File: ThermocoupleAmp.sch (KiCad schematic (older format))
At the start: 7 parts

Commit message: Done with preliminary schematic. Needs review
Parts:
- C602: renamed from C?; footprint (none) -> Capacitor_SMD:C_0603_1608Metric
- R601, R602, R603: renamed from R?; footprint (none) -> Resistor_SMD:R_0603_1608Metric
- gave numbers to parts that had none: 3
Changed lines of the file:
@@
 $Descr A4 11693 8268
 encoding utf-8
-Sheet 7 7
+Sheet 6 7
 Title ""
 Date ""
@@
 $EndDescr
 $Comp
-L ReflowOven:MCP96RL01T U?
+L ReflowOven:MCP96RL01T U601
 U 1 1 5F712CB5
 P 5650 3250
-F 0 "U?" H 5650 3815 50  0000 C CNN
+F 0 "U601" H 5650 3815 50  0000 C CNN
 F 1 "MCP96RL01T" H 5650 3724 50  0000 C CNN
 F 2 "" H 5600 3500 50  0001 C CNN
@@
 	4900 2950 4900 2800
 $Comp
-L power:+3.3VA #PWR?
+L power:+3.3VA #PWR0603
 U 1 1 5F716651
 P 4900 2800
-F 0 "#PWR?" H 4900 2650 50  0001 C CNN
+F 0 "#PWR0603" H 4900 2650 50  0001 C CNN
 F 1 "+3.3VA" H 4915 2973 50  0000 C CNN
 F 2 "" H 4900 2800 50  0001 C CNN
@@
 $EndComp
 $Comp
-L power:GNDA #PWR?
+L power:GNDA #PWR0608
 U 1 1 5F7169A0
 P 4900 4300
-F 0 "#PWR?" H 4900 4050 50  0001 C CNN
+F 0 "#PWR0608" H 4900 4050 50  0001 C CNN
 F 1 "GNDA" H 4905 4127 50  0000 C CNN
 F 2 "" H 4900 4300 50  0001 C CNN
@@
 $EndComp
 $Comp
-L Connector:Conn_01x02_Male J?
+L Connector:Conn_01x02_Male J601
 U 1 1 5F71786F
 P 7300 4050
-F 0 "J?" H 7272 3932 50  0000 R CNN
+F 0 "J601" H 7272 3932 50  0000 R CNN
 F 1 "Conn_01x02_Male" H 7272 4023 50  0000 R CNN
 F 2 "" H 7300 4050 50  0001 C CNN
@@
 NoConn ~ 6250 2950
 $Comp
-L power:+3.3VA #PWR?
+L power:+3.3VA #PWR0606
 U 1 1 5F71AC1D
 P 6500 3200
-F 0 "#PWR?" H 6500 3050 50  0001 C CNN
+F 0 "#PWR0606" H 6500 3050 50  0001 C CNN
 F 1 "+3.3VA" H 6515 3373 50  0000 C CNN
 F 2 "" H 6500 3200 50  0001 C CNN
@@
 	6500 3200 6500 3250
 $Comp
-L Device:R_Small R?
+L Device:R_Small R601
 U 1 1 5F71B54E
 P 6500 3350
-F 0 "R?" H 6559 3396 50  0000 L CNN
+F 0 "R601" H 6559 3396 50  0000 L CNN
 F 1 "1M" H 6559 3305 50  0000 L CNN
-F 2 "" H 6500 3350 50  0001 C CNN
+F 2 "Resistor_SMD:R_0603_1608Metric" H 6500 3350 50  0001 C CNN
 F 3 "~" H 6500 3350 50  0001 C CNN
 	1    6500 3350
@@
 	6800 4050 7100 4050
 $Comp
-L Device:R_Small R?
+L Device:R_Small R603
 U 1 1 5F71BB42
 P 6800 4250
-F 0 "R?" H 6859 4296 50  0000 L CNN
+F 0 "R603" H 6859 4296 50  0000 L CNN
 F 1 "2M" H 6859 4205 50  0000 L CNN
-F 2 "" H 6800 4250 50  0001 C CNN
+F 2 "Resistor_SMD:R_0603_1608Metric" H 6800 4250 50  0001 C CNN
 F 3 "~" H 6800 4250 50  0001 C CNN
 	1    6800 4250
@@
 $EndComp
 $Comp
-L Device:R_Small R?
+L Device:R_Small R602
 U 1 1 5F71BF24
 P 6800 3600
-F 0 "R?" V 6604 3600 50  0000 C CNN
+F 0 "R602" V 6604 3600 50  0000 C CNN
 F 1 "2M" V 6695 3600 50  0000 C CNN
-F 2 "" H 6800 3600 50  0001 C CNN
+F 2 "Resistor_SMD:R_0603_1608Metric" H 6800 3600 50  0001 C CNN
 F 3 "~" H 6800 3600 50  0001 C CNN
 	1    6800 3600
@@
 	6500 3600 6700 3600
 $Comp
-L power:GNDA #PWR?
+L power:GNDA #PWR0607
 U 1 1 5F71CF5F
 P 7000 3700
-F 0 "#PWR?" H 7000 3450 50  0001 C CNN
+F 0 "#PWR0607" H 7000 3450 50  0001 C CNN
 F 1 "GNDA" H 7005 3527 50  0000 C CNN
 F 2 "" H 7000 3700 50  0001 C CNN
@@
 	6800 4350 6800 4450
 $Comp
-L power:GNDA #PWR?
+L power:GNDA #PWR0609
 U 1 1 5F720547
 P 6800 4450
-F 0 "#PWR?" H 6800 4200 50  0001 C CNN
+F 0 "#PWR0609" H 6800 4200 50  0001 C CNN
 F 1 "GNDA" H 6805 4277 50  0000 C CNN
 F 2 "" H 6800 4450 50  0001 C CNN
@@
 $EndComp
 $Comp
-L Device:C_Small C?
+L Device:C_Small C602
 U 1 1 5F73439B
 P 4500 2650
-F 0 "C?" H 4592 2696 50  0000 L CNN
+F 0 "C602" H 4592 2696 50  0000 L CNN
 F 1 "0.1u" H 4592 2605 50  0000 L CNN
-F 2 "" H 4500 2650 50  0001 C CNN
+F 2 "Capacitor_SMD:C_0603_1608Metric" H 4500 2650 50  0001 C CNN
 F 3 "~" H 4500 2650 50  0001 C CNN
 	1    4500 2650
@@
 $EndComp
 $Comp
-L Device:C_Small C?
+L Device:C_Small C601
 U 1 1 5F7344CC
 P 4150 2650
-F 0 "C?" H 4059 2604 50  0000 R CNN
+F 0 "C601" H 4059 2604 50  0000 R CNN
 F 1 "10uF" H 4059 2695 50  0000 R CNN
 F 2 "" H 4150 2650 50  0001 C CNN
@@
 	4150 2750 4150 2850
 $Comp
-L power:+3.3VA #PWR?
+L power:+3.3VA #PWR0602
 U 1 1 5F7356C0
 P 4500 2450
-F 0 "#PWR?" H 4500 2300 50  0001 C CNN
+F 0 "#PWR0602" H 4500 2300 50  0001 C CNN
 F 1 "+3.3VA" H 4515 2623 50  0000 C CNN
 F 2 "" H 4500 2450 50  0001 C CNN
@@
 $EndComp
 $Comp
-L power:+3.3VA #PWR?
+L power:+3.3VA #PWR0601
 U 1 1 5F735ABE
 P 4150 2450
-F 0 "#PWR?" H 4150 2300 50  0001 C CNN
+F 0 "#PWR0601" H 4150 2300 50  0001 C CNN
 F 1 "+3.3VA" H 4165 2623 50  0000 C CNN
 F 2 "" H 4150 2450 50  0001 C CNN
@@
 	4500 2850 4500 2750
 $Comp
-L power:GNDA #PWR?
+L power:GNDA #PWR0605
 U 1 1 5F736899
 P 4500 2850
-F 0 "#PWR?" H 4500 2600 50  0001 C CNN
+F 0 "#PWR0605" H 4500 2600 50  0001 C CNN
 F 1 "GNDA" H 4505 2677 50  0000 C CNN
 F 2 "" H 4500 2850 50  0001 C CNN
@@
 $EndComp
 $Comp
-L power:GNDA #PWR?
+L power:GNDA #PWR0604
 U 1 1 5F736AC2
 P 4150 2850
-F 0 "#PWR?" H 4150 2600 50  0001 C CNN
+F 0 "#PWR0604" H 4150 2600 50  0001 C CNN
 F 1 "GNDA" H 4155 2677 50  0000 C CNN
 F 2 "" H 4150 2850 50  0001 C CNN

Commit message: Added stuff
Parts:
- C601: value 10uF -> 10u; footprint (none) -> Capacitor_SMD:C_0603_1608Metric
- J601: value Conn_01x02_Male -> Thermocouple_Conn
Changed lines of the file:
@@
 P 7300 4050
 F 0 "J601" H 7272 3932 50  0000 R CNN
-F 1 "Conn_01x02_Male" H 7272 4023 50  0000 R CNN
+F 1 "Thermocouple_Conn" H 7272 4023 50  0000 R CNN
 F 2 "" H 7300 4050 50  0001 C CNN
 F 3 "~" H 7300 4050 50  0001 C CNN
@@
 P 4150 2650
 F 0 "C601" H 4059 2604 50  0000 R CNN
-F 1 "10uF" H 4059 2695 50  0000 R CNN
-F 2 "" H 4150 2650 50  0001 C CNN
+F 1 "10u" H 4059 2695 50  0000 R CNN
+F 2 "Capacitor_SMD:C_0603_1608Metric" H 4150 2650 50  0001 C CNN
 F 3 "~" H 4150 2650 50  0001 C CNN
 	1    4150 2650

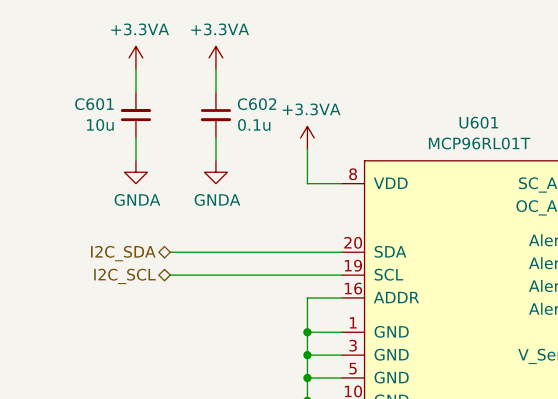
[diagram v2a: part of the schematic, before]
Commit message: Added some footprints
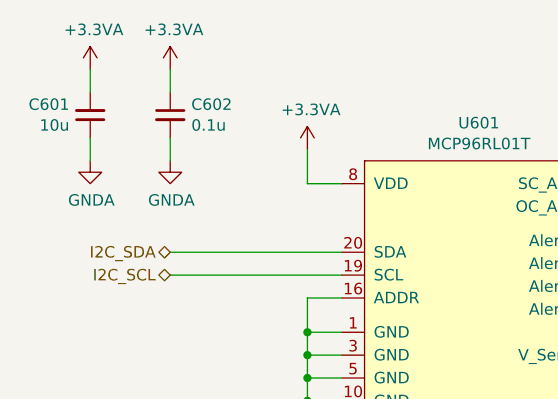
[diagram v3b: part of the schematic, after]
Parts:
- U601: footprint (none) -> ReflowOven:QFN-20_EP_5x5_Pitch0.65mm
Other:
- moved on the sheet: C601, C602
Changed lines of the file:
@@
 F 0 "U601" H 5650 3815 50  0000 C CNN
 F 1 "MCP96RL01T" H 5650 3724 50  0000 C CNN
-F 2 "" H 5600 3500 50  0001 C CNN
+F 2 "ReflowOven:QFN-20_EP_5x5_Pitch0.65mm" H 5600 3500 50  0001 C CNN
 F 3 "" H 5600 3500 50  0001 C CNN
 	1    5650 3250
@@
 L Device:C_Small C602
 U 1 1 5F73439B
-P 4500 2650
-F 0 "C602" H 4592 2696 50  0000 L CNN
-F 1 "0.1u" H 4592 2605 50  0000 L CNN
-F 2 "Capacitor_SMD:C_0603_1608Metric" H 4500 2650 50  0001 C CNN
-F 3 "~" H 4500 2650 50  0001 C CNN
-	1    4500 2650
+P 4300 2650
+F 0 "C602" H 4392 2696 50  0000 L CNN
+F 1 "0.1u" H 4392 2605 50  0000 L CNN
+F 2 "Capacitor_SMD:C_0603_1608Metric" H 4300 2650 50  0001 C CNN
+F 3 "~" H 4300 2650 50  0001 C CNN
+	1    4300 2650
 	1    0    0    -1
 $EndComp
@@
 L Device:C_Small C601
 U 1 1 5F7344CC
-P 4150 2650
-F 0 "C601" H 4059 2604 50  0000 R CNN
-F 1 "10u" H 4059 2695 50  0000 R CNN
-F 2 "Capacitor_SMD:C_0603_1608Metric" H 4150 2650 50  0001 C CNN
-F 3 "~" H 4150 2650 50  0001 C CNN
-	1    4150 2650
+P 3950 2650
+F 0 "C601" H 3859 2604 50  0000 R CNN
+F 1 "10u" H 3859 2695 50  0000 R CNN
+F 2 "Capacitor_SMD:C_0603_1608Metric" H 3950 2650 50  0001 C CNN
+F 3 "~" H 3950 2650 50  0001 C CNN
+	1    3950 2650
 	1    0    0    1
 $EndComp
 Wire Wire Line
-	4500 2550 4500 2450
-Wire Wire Line
-	4150 2450 4150 2550
-Wire Wire Line
-	4150 2750 4150 2850
+	4300 2550 4300 2450
+Wire Wire Line
+	3950 2450 3950 2550
+Wire Wire Line
+	3950 2750 3950 2850
 $Comp
 L power:+3.3VA #PWR0602
 U 1 1 5F7356C0
-P 4500 2450
-F 0 "#PWR0602" H 4500 2300 50  0001 C CNN
-F 1 "+3.3VA" H 4515 2623 50  0000 C CNN
-F 2 "" H 4500 2450 50  0001 C CNN
-F 3 "" H 4500 2450 50  0001 C CNN
-	1    4500 2450
+P 4300 2450
+F 0 "#PWR0602" H 4300 2300 50  0001 C CNN
+F 1 "+3.3VA" H 4315 2623 50  0000 C CNN
+F 2 "" H 4300 2450 50  0001 C CNN
+F 3 "" H 4300 2450 50  0001 C CNN
+	1    4300 2450
 	1    0    0    -1
 $EndComp
@@
 L power:+3.3VA #PWR0601
 U 1 1 5F735ABE
-P 4150 2450
-F 0 "#PWR0601" H 4150 2300 50  0001 C CNN
-F 1 "+3.3VA" H 4165 2623 50  0000 C CNN
-F 2 "" H 4150 2450 50  0001 C CNN
-F 3 "" H 4150 2450 50  0001 C CNN
-	1    4150 2450
-	1    0    0    -1
-$EndComp
-Wire Wire Line
-	4500 2850 4500 2750
+P 3950 2450
+F 0 "#PWR0601" H 3950 2300 50  0001 C CNN
+F 1 "+3.3VA" H 3965 2623 50  0000 C CNN
+F 2 "" H 3950 2450 50  0001 C CNN
+F 3 "" H 3950 2450 50  0001 C CNN
+	1    3950 2450
+	1    0    0    -1
+$EndComp
+Wire Wire Line
+	4300 2850 4300 2750
 $Comp
 L power:GNDA #PWR0605
 U 1 1 5F736899
-P 4500 2850
-F 0 "#PWR0605" H 4500 2600 50  0001 C CNN
-F 1 "GNDA" H 4505 2677 50  0000 C CNN
-F 2 "" H 4500 2850 50  0001 C CNN
-F 3 "" H 4500 2850 50  0001 C CNN
-	1    4500 2850
+P 4300 2850
+F 0 "#PWR0605" H 4300 2600 50  0001 C CNN
+F 1 "GNDA" H 4305 2677 50  0000 C CNN
+F 2 "" H 4300 2850 50  0001 C CNN
+F 3 "" H 4300 2850 50  0001 C CNN
+	1    4300 2850
 	1    0    0    -1
 $EndComp
@@
 L power:GNDA #PWR0604
 U 1 1 5F736AC2
-P 4150 2850
-F 0 "#PWR0604" H 4150 2600 50  0001 C CNN
-F 1 "GNDA" H 4155 2677 50  0000 C CNN
-F 2 "" H 4150 2850 50  0001 C CNN
-F 3 "" H 4150 2850 50  0001 C CNN
-	1    4150 2850
-	1    0    0    -1
-$EndComp
+P 3950 2850
+F 0 "#PWR0604" H 3950 2600 50  0001 C CNN
+F 1 "GNDA" H 3955 2677 50  0000 C CNN
+F 2 "" H 3950 2850 50  0001 C CNN
+F 3 "" H 3950 2850 50  0001 C CNN
+	1    3950 2850
+	1    0    0    -1
+$EndComp
